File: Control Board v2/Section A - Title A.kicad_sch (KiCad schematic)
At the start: 0 parts

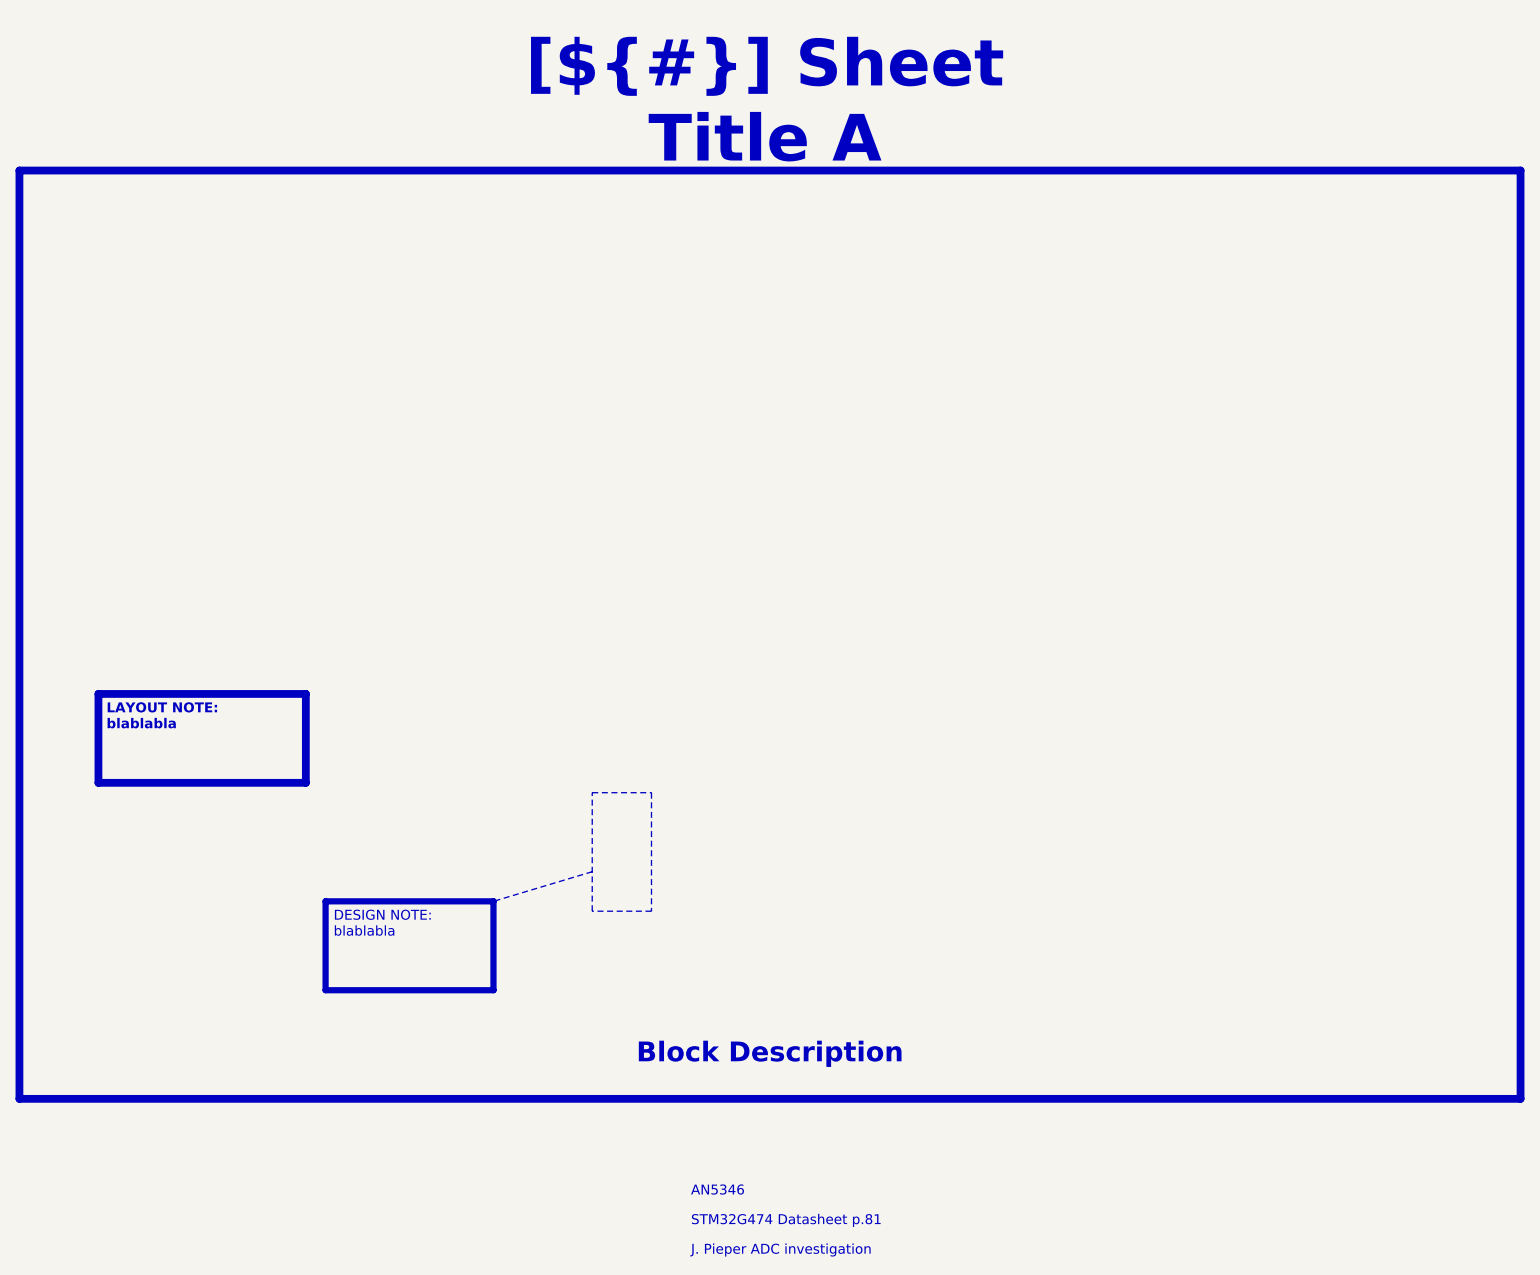
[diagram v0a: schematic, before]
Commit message: Finish preparing the template for v2 design
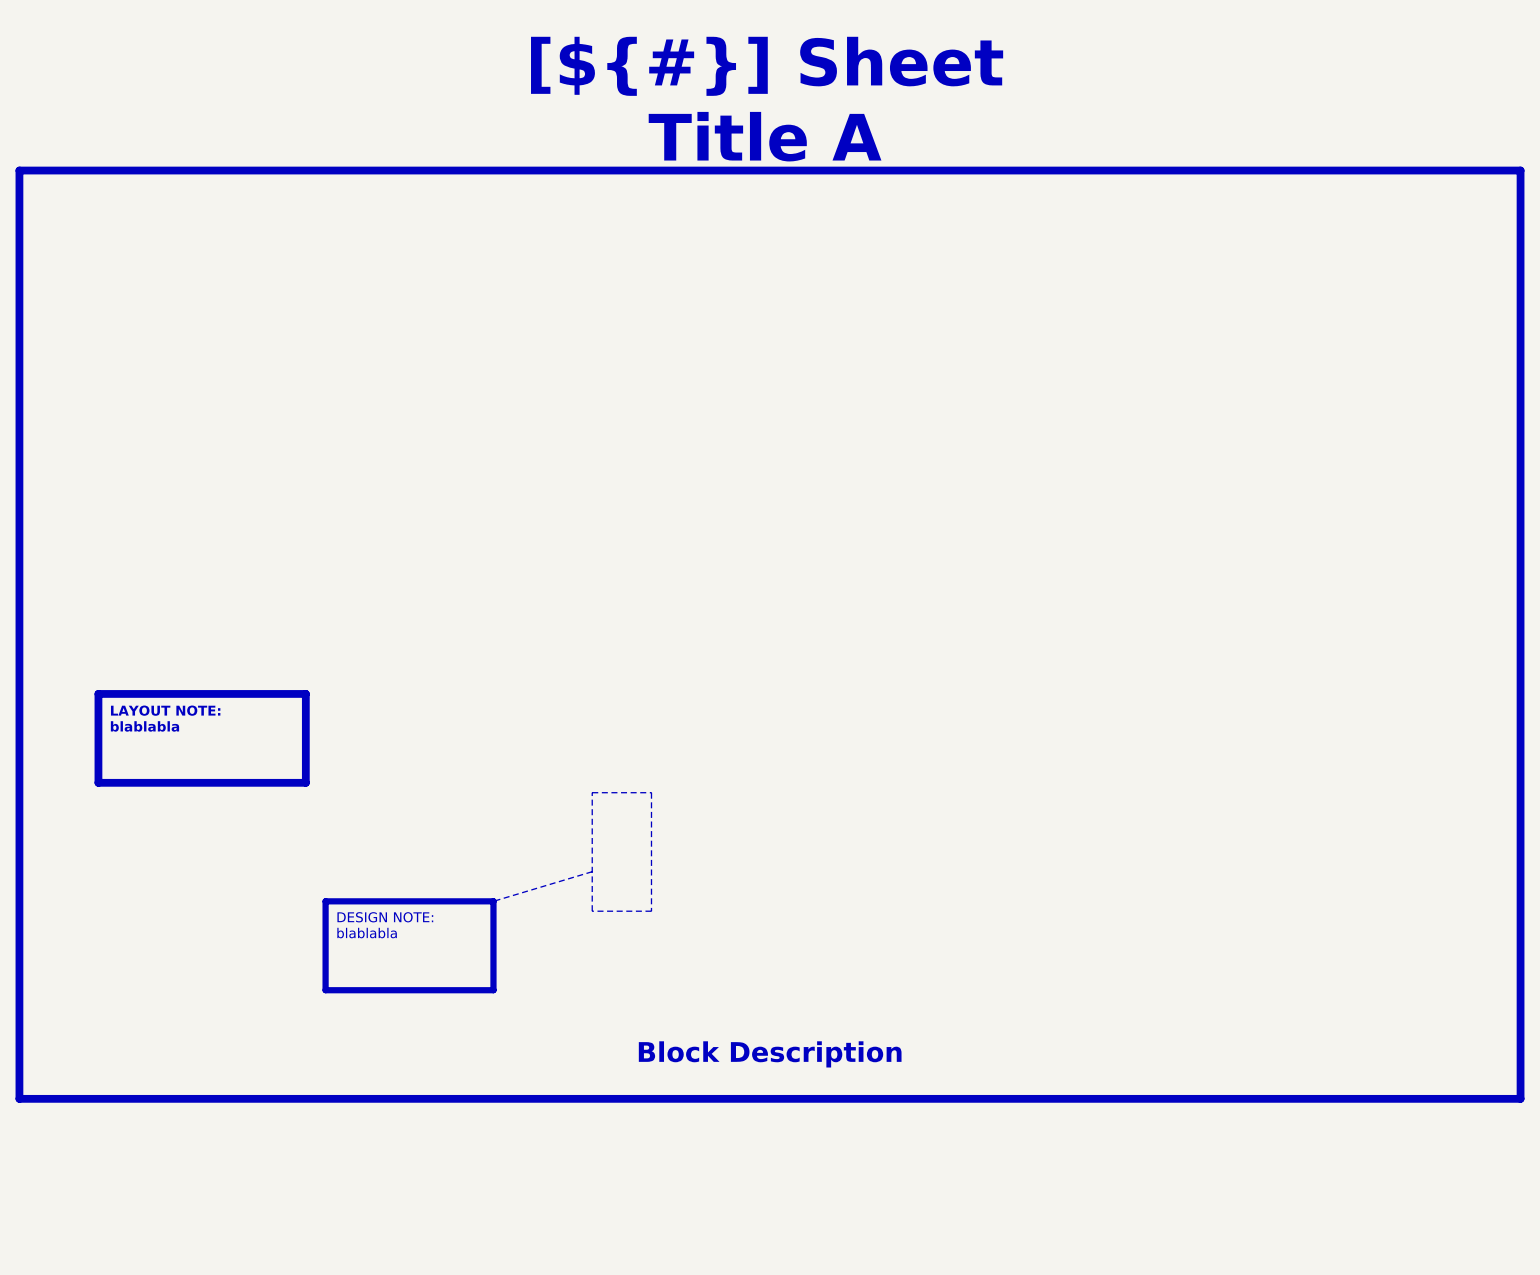
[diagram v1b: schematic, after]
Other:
- note removed: "AN5346"
- note removed: "J. Pieper ADC investigation"
- note removed: "STM32G474 Datasheet p.81"
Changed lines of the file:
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@@
 (kicad_sch
-	(version 20231120)
+	(version 20250114)
 	(generator "eeschema")
-	(generator_version "8.0")
+	(generator_version "9.0")
 	(paper "A4")
 	(title_block
 		(title "Sheet Title A")
-		(date "Last Modified Date")
+		(date "2025-08-28")
 		(rev "${REVISION}")
 		(company "${COMPANY}")
-	)
-	(polyline
-		(pts
-			(xy 129.54 120.65) (xy 116.84 124.46)
-		)
-		(stroke
-			(width 0)
-			(type dot)
-			(color 255 0 0 1)
-		)
 	)
 	(rectangle
@@
 		(at 66.04 97.79 0)
 		(size 26.67 11.43)
+		(margins 1.4525 1.4525 1.4525 1.4525)
 		(stroke
 			(width 1)
@@
 		(at 115.57 15.24 0)
 		(size 72.39 12.7)
+		(margins 4.4999 4.4999 4.4999 4.4999)
 		(stroke
 			(width -0.0001)
@@
 		(at 57.15 139.7 0)
 		(size 190.5 7.62)
+		(margins 1.9049 1.9049 1.9049 1.9049)
 		(stroke
 			(width -0.0001)
@@
 		(at 95.25 124.46 0)
 		(size 21.59 11.43)
+		(margins 1.3525 1.3525 1.3525 1.3525)
 		(stroke
 			(width 0.8)
@@
 		)
 	)
-	(text "J. Pieper ADC investigation"
-		(exclude_from_sim no)
-		(at 142.24 170.18 0)
-		(effects
-			(font
-				(face "Arial")
-				(size 1.27 1.27)
-				(color 0 0 0 1)
-			)
-			(justify left bottom)
-			(href "https://jpieper.com/2023/07/24/stm32g4-adc-performance-part-2/")
+	(polyline
+		(pts
+			(xy 129.54 120.65) (xy 116.84 124.46)
+		)
+		(stroke
+			(width 0)
+			(type dot)
+			(color 255 0 0 1)
 		)
 	)
-	(text "STM32G474 Datasheet p.81"
-		(exclude_from_sim no)
-		(at 142.24 166.37 0)
-		(effects
-			(font
-				(face "Arial")
-				(size 1.27 1.27)
-				(color 0 0 0 1)
-			)
-			(justify left bottom)
-			(href "https://www.st.com/resource/en/datasheet/stm32g474cb.pdf")
-		)
-	)
-	(text "AN5346"
-		(exclude_from_sim no)
-		(at 142.24 162.56 0)
-		(effects
-			(font
-				(face "Arial")
-				(size 1.27 1.27)
-				(color 0 0 0 1)
-			)
-			(justify left bottom)
-			(href "https://www.st.com/resource/en/application_note/an5346-stm32g4-adc-use-tips-and-recommendations-stmicroelectronics.pdf")
-		)
-	)
